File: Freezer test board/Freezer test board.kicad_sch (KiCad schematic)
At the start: 19 parts, among them J2 Conn_02x20_Odd_Even, J3 284391-3, J4 284391-3, J5 284391-3, J6 284391-3, J7 284391-3, J8 284391-3, J9 284391-3

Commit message: Adjust mounting hole footprint to 2.7mm M2.5
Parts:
- H1, H2, H3, H4: footprint MountingHole:MountingHole_2.5mm_Pad -> MountingHole:MountingHole_2.7mm_M2.5_Pad
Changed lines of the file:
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@@
 			)
 		)
-		(property "Footprint" "MountingHole:MountingHole_2.5mm_Pad"
+		(property "Footprint" "MountingHole:MountingHole_2.7mm_M2.5_Pad"
 			(at 85.09 49.53 0)
 			(effects
@@
 			)
 		)
-		(property "Footprint" "MountingHole:MountingHole_2.5mm_Pad"
+		(property "Footprint" "MountingHole:MountingHole_2.7mm_M2.5_Pad"
 			(at 85.09 30.48 0)
 			(effects
@@
 			)
 		)
-		(property "Footprint" "MountingHole:MountingHole_2.5mm_Pad"
+		(property "Footprint" "MountingHole:MountingHole_2.7mm_M2.5_Pad"
 			(at 85.09 43.18 0)
 			(effects
@@
 			)
 		)
-		(property "Footprint" "MountingHole:MountingHole_2.5mm_Pad"
+		(property "Footprint" "MountingHole:MountingHole_2.7mm_M2.5_Pad"
 			(at 85.09 36.83 0)
 			(effects

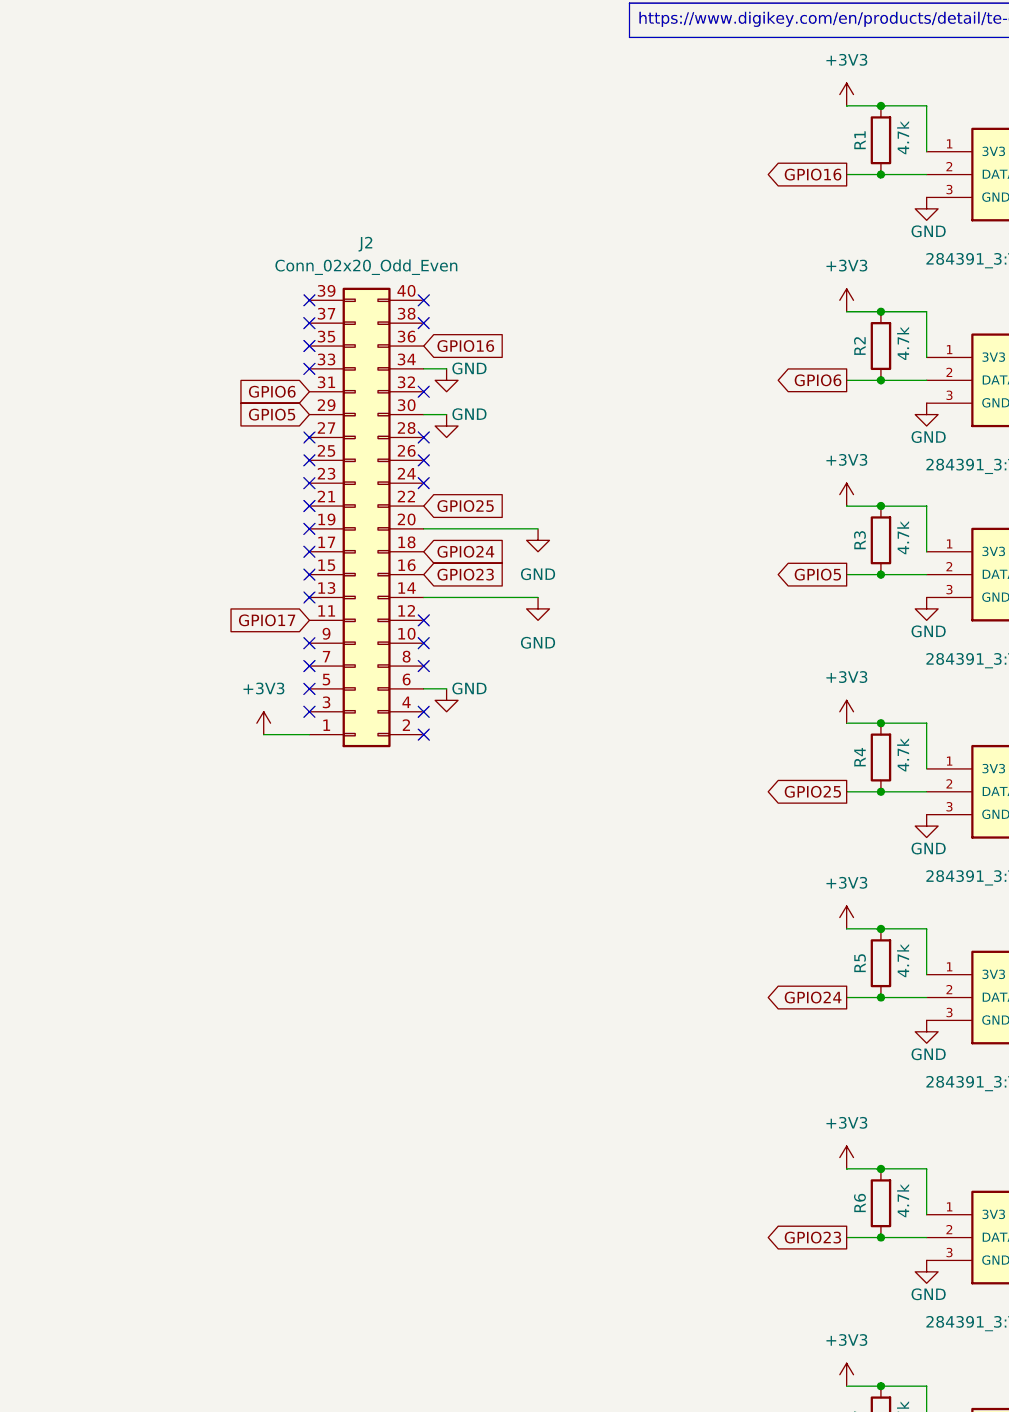
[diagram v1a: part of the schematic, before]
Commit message: V1.1
Revised the pin out for the traces 10 times and got a second opinion. they are all connected properly. added more memes, adjusted the text indicating what pin is what, added text for the 3V3 pin, Ensure that spacing is correct, and updated the schematic and picture of the schematic on the board
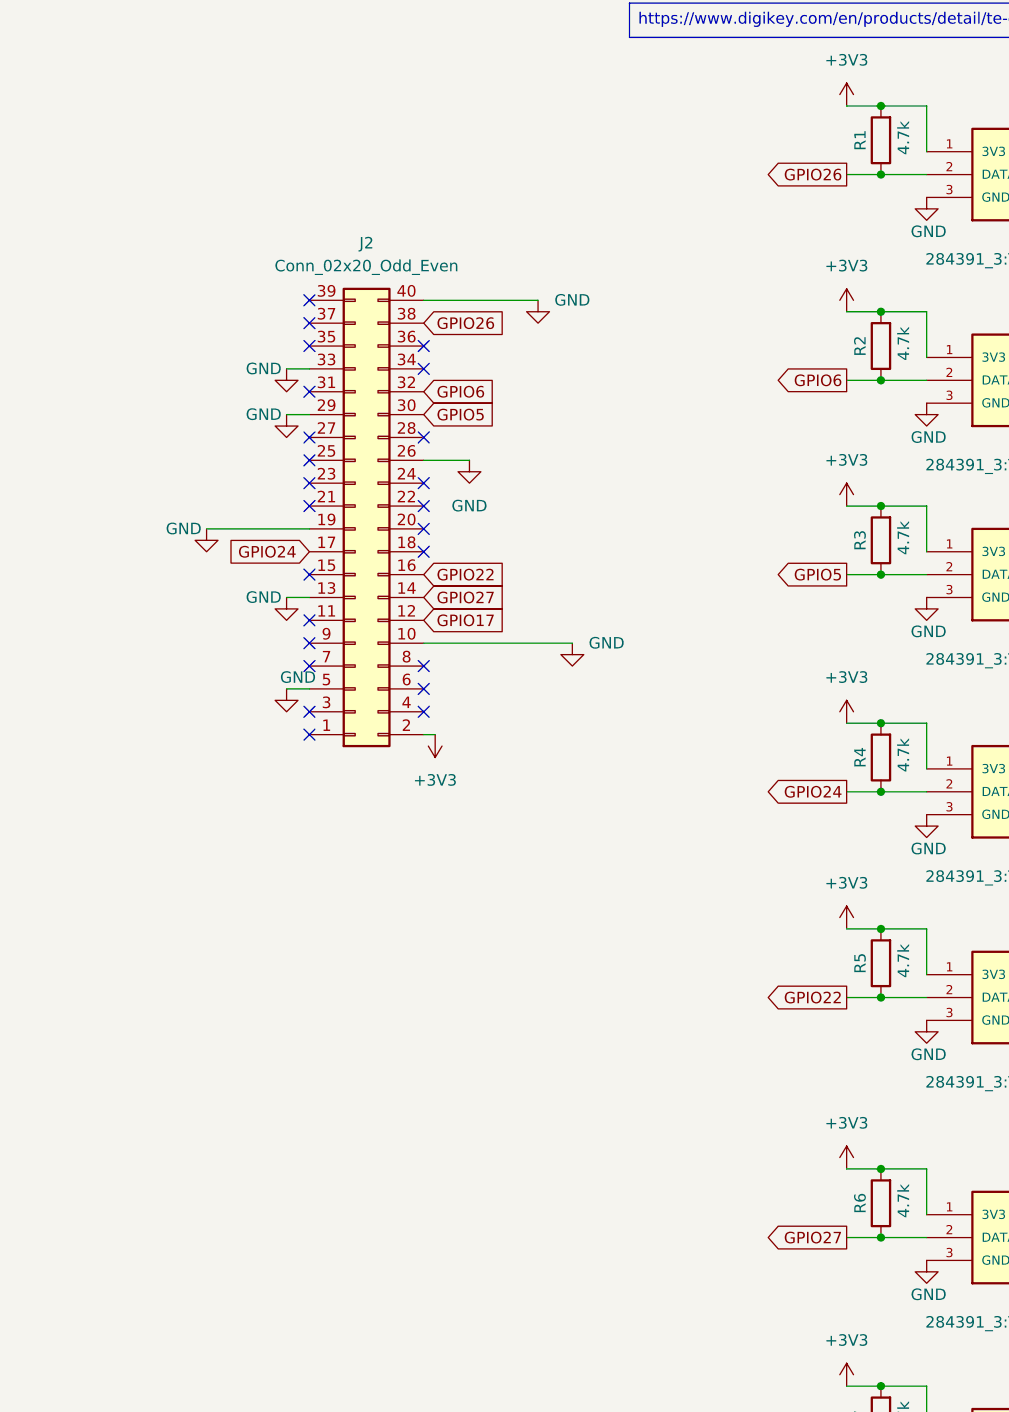
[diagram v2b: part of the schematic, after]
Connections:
- net +3V3: now also J2.2 (Pin_2); no longer J2.1 (pin_1)
- net GND: now also J2.10 (Pin_10), J2.13 (Pin_13), J2.19 (Pin_19), J2.26 (Pin_26), J2.29 (Pin_29), J2.33 (Pin_33), J2.40 (Pin_40), J2.5 (Pin_5); no longer J2.14 (Pin_14), J2.20 (Pin_20), J2.30 (Pin_30), J2.34 (Pin_34), J2.6 (Pin_6)
- net GPIO17: now also J2.12 (Pin_12); no longer J2.11 (Pin_11)
- net GPIO24: now also J2.17 (Pin_17), J6.2 (DATA), R4.1; no longer J2.18 (Pin_18), J7.2 (DATA), R5.1
- net GPIO5: now also J2.30 (Pin_30); no longer J2.29 (Pin_29)
- net GPIO6: now also J2.32 (Pin_32); no longer J2.31 (Pin_31)
- net GPIO26: now reaches J2.38 (Pin_38)
- net GPIO26: now also J3.2 (DATA), R1.1
- removed net GPIO16: J2.36 (Pin_36), J3.2 (DATA), R1.1
- net GPIO23 renamed GPIO27
- net GPIO27: now also J2.14 (Pin_14); no longer J2.16 (Pin_16)
- removed net GPIO25: J2.22 (Pin_22), J6.2 (DATA), R4.1
- new net GPIO22: J2.16 (Pin_16), J7.2 (DATA), R5.1
- no-connect marks 27 -> 24
